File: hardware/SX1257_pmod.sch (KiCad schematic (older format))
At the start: 55 parts, among them J1 Conn_02x06_Odd_Even, J2 SMA_F_RX, J3 SMA_F_TX, U1 SX1257, U2 SC18IS602B, Y1 32/36MHz ?ppm

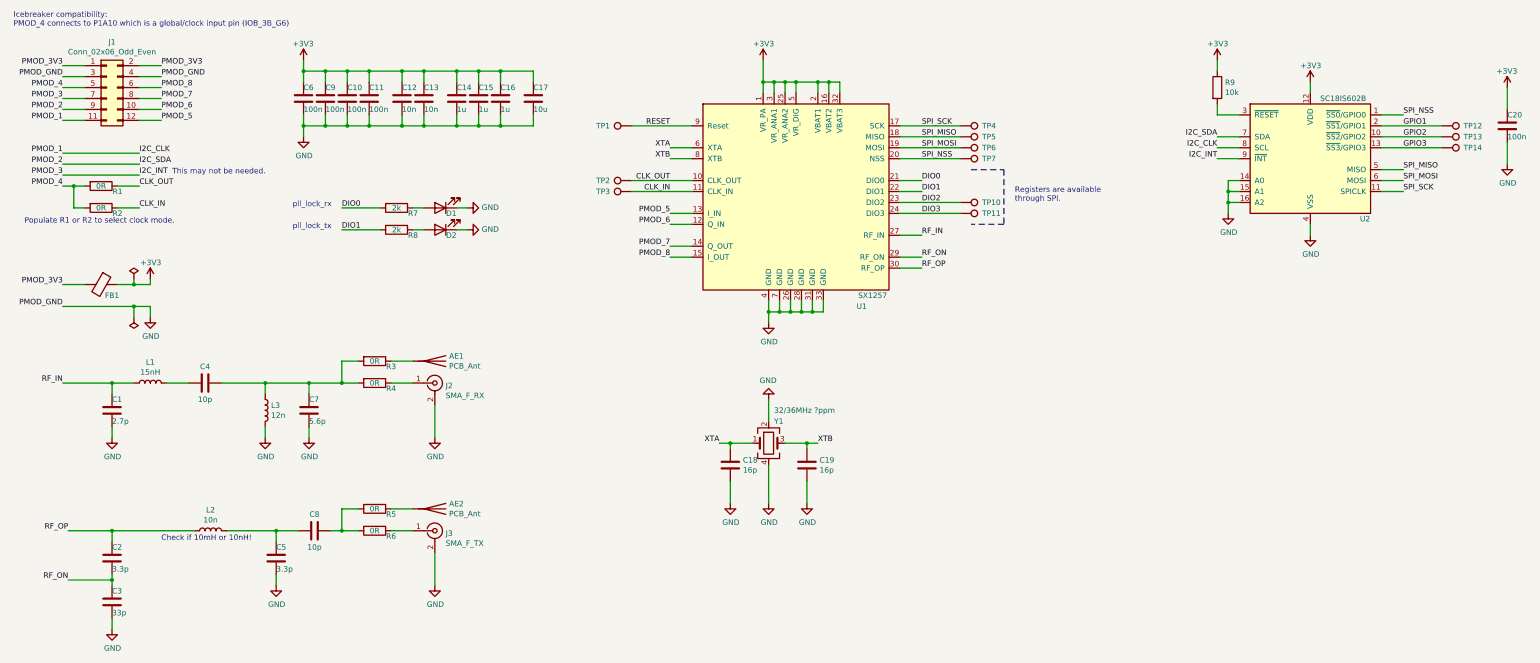
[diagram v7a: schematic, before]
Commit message: Some improvements and pcb work
- Connected gpio1 to SX_RESET
- Removed R0 for CLK select
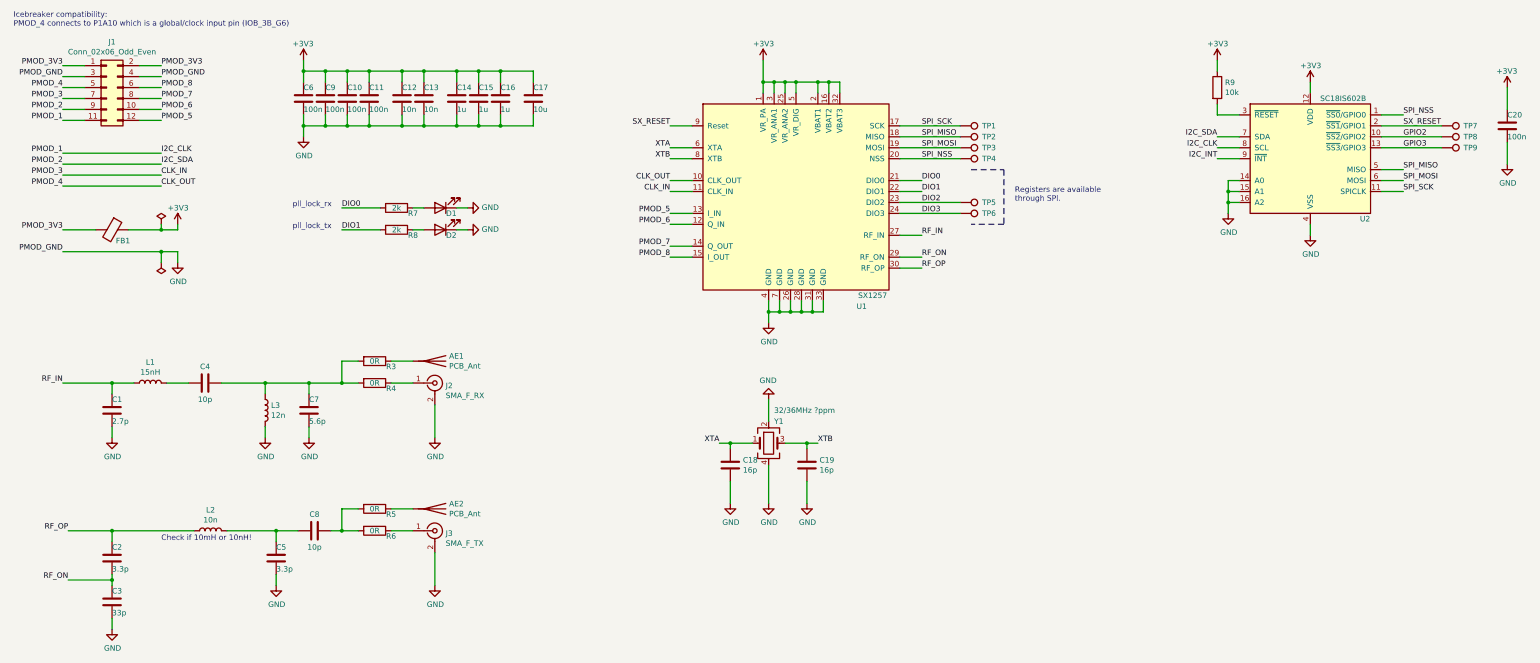
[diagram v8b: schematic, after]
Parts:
- removed R1, R2: 0R, Resistor_SMD:R_0603_1608Metric, symbol Device:R
- removed TP1, TP2, TP3: TestPoint, TestPoint:TestPoint_Pad_D1.0mm, symbol Connector:TestPoint
- renumbered TP4 to TP1, TP5 to TP2, TP6 to TP3, TP7 to TP4, TP10 to TP5, TP11 to TP6, TP12 to TP7, TP13 to TP8, TP14 to TP9
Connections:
- net PMOD_4 is gone; now on net CLK_OUT: J1.5 (Pin_5)
- net RESET is gone; now on net SX_RESET: U1.9 (Reset)
- net CLK_IN: now also J1.7 (Pin_7)
- net I2C_INT: no longer J1.7 (Pin_7)
- net GPIO1 renamed SX_RESET
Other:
- note removed: "Populate R1 or R2 to select clock mode."
- note removed: "This may not be needed."
- moved on the sheet: FB1
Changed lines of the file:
@@
 Text Label 1000 2150 2    50   ~ 0
 PMOD_4
-$Comp
-L Device:R R1
-U 1 1 5C2B7109
-P 1350 2150
-F 0 "R1" V 1400 2300 50  0000 C CNN
-F 1 "0R" V 1350 2150 50  0000 C CNN
-F 2 "Resistor_SMD:R_0603_1608Metric" V 1280 2150 50  0001 C CNN
-F 3 "~" H 1350 2150 50  0001 C CNN
-	1    1350 2150
-	0    1    1    0
-$EndComp
-Text Label 1700 2350 0    50   ~ 0
+Text Label 1900 2050 0    50   ~ 0
 CLK_IN
-Wire Wire Line
-	1000 2150 1100 2150
-Wire Wire Line
-	1500 2150 1700 2150
 Wire Wire Line
 	6750 1800 6550 1800
@@
 Wire Wire Line
 	1000 1050 1200 1050
-Text Label 1000 3050 2    50   ~ 0
+Text Label 1000 2550 2    50   ~ 0
 PMOD_3V3
 $Comp
 L Device:Ferrite_Bead FB1
 U 1 1 5C30A1D4
-P 1350 3050
-F 0 "FB1" V 1450 3150 50  0000 C CNN
-F 1 "Ferrite_Bead" V 1150 3000 50  0001 C CNN
-F 2 "Inductor_SMD:L_0603_1608Metric" V 1280 3050 50  0001 C CNN
-F 3 "~" H 1350 3050 50  0001 C CNN
-	1    1350 3050
-	0    1    1    0
-$EndComp
-Wire Wire Line
-	1000 3050 1200 3050
+P 1450 2550
+F 0 "FB1" V 1550 2650 50  0000 C CNN
+F 1 "Ferrite_Bead" V 1250 2500 50  0001 C CNN
+F 2 "Inductor_SMD:L_0603_1608Metric" V 1380 2550 50  0001 C CNN
+F 3 "~" H 1450 2550 50  0001 C CNN
+	1    1450 2550
+	0    1    1    0
+$EndComp
+Wire Wire Line
+	1000 2550 1300 2550
 $Comp
 L power:+3V3 #PWR03
 U 1 1 5C30B964
-P 1800 3000
-F 0 "#PWR03" H 1800 2850 50  0001 C CNN
-F 1 "+3V3" H 1700 3150 50  0000 L CNN
-F 2 "" H 1800 3000 50  0001 C CNN
-F 3 "" H 1800 3000 50  0001 C CNN
-	1    1800 3000
+P 2050 2500
+F 0 "#PWR03" H 2050 2350 50  0001 C CNN
+F 1 "+3V3" H 1950 2650 50  0000 L CNN
+F 2 "" H 2050 2500 50  0001 C CNN
+F 3 "" H 2050 2500 50  0001 C CNN
+	1    2050 2500
 	-1   0    0    -1
 $EndComp
@@
 L power:PWR_FLAG #FLG01
 U 1 1 5C3103FC
-P 1650 3000
-F 0 "#FLG01" H 1650 3075 50  0001 C CNN
-F 1 "PWR_FLAG" H 1650 3174 50  0001 C CNN
-F 2 "" H 1650 3000 50  0001 C CNN
-F 3 "~" H 1650 3000 50  0001 C CNN
-	1    1650 3000
-	1    0    0    -1
-$EndComp
-Wire Wire Line
-	1650 3000 1650 3050
-Connection ~ 1650 3050
-Wire Wire Line
-	1650 3050 1500 3050
-Wire Wire Line
-	1800 3050 1800 3000
-Wire Wire Line
-	1650 3050 1800 3050
+P 1900 2500
+F 0 "#FLG01" H 1900 2575 50  0001 C CNN
+F 1 "PWR_FLAG" H 1900 2674 50  0001 C CNN
+F 2 "" H 1900 2500 50  0001 C CNN
+F 3 "~" H 1900 2500 50  0001 C CNN
+	1    1900 2500
+	1    0    0    -1
+$EndComp
+Wire Wire Line
+	1900 2500 1900 2550
+Connection ~ 1900 2550
+Wire Wire Line
+	2050 2550 2050 2500
+Wire Wire Line
+	1900 2550 2050 2550
 Text Label 8850 2100 0    50   ~ 0
 DIO0
@@
 DIO3
 $Comp
-L Connector:TestPoint TP10
+L Connector:TestPoint TP5
 U 1 1 5C32BD15
 P 9200 2300
-F 0 "TP10" V 9200 2500 50  0000 L CNN
+F 0 "TP5" V 9200 2500 50  0000 L CNN
 F 1 "TestPoint" V 9200 2750 50  0001 L CNN
 F 2 "TestPoint:TestPoint_Pad_D1.0mm" H 9400 2300 50  0001 C CNN
@@
 $EndComp
 $Comp
-L Connector:TestPoint TP11
+L Connector:TestPoint TP6
 U 1 1 5C32DD47
 P 9200 2400
-F 0 "TP11" V 9200 2600 50  0000 L CNN
+F 0 "TP6" V 9200 2600 50  0000 L CNN
 F 1 "TestPoint" V 9200 2850 50  0001 L CNN
 F 2 "TestPoint:TestPoint_Pad_D1.0mm" H 9400 2400 50  0001 C CNN
@@
 L power:PWR_FLAG #FLG02
 U 1 1 5C3953E6
-P 1650 3350
-F 0 "#FLG02" H 1650 3425 50  0001 C CNN
-F 1 "PWR_FLAG" H 1650 3524 50  0001 C CNN
-F 2 "" H 1650 3350 50  0001 C CNN
-F 3 "~" H 1650 3350 50  0001 C CNN
-	1    1650 3350
+P 1900 2850
+F 0 "#FLG02" H 1900 2925 50  0001 C CNN
+F 1 "PWR_FLAG" H 1900 3024 50  0001 C CNN
+F 2 "" H 1900 2850 50  0001 C CNN
+F 3 "~" H 1900 2850 50  0001 C CNN
+	1    1900 2850
 	-1   0    0    1
 $EndComp
-$Comp
-L Connector:TestPoint TP1
-U 1 1 5C39E2AB
-P 6200 1600
-F 0 "TP1" V 6200 1800 50  0000 L CNN
-F 1 "TestPoint" V 6200 2050 50  0001 L CNN
-F 2 "TestPoint:TestPoint_Pad_D1.0mm" H 6400 1600 50  0001 C CNN
-F 3 "~" H 6400 1600 50  0001 C CNN
-	1    6200 1600
-	0    -1   -1   0
-$EndComp
-Text Label 6550 1600 2    50   ~ 0
-RESET
 Wire Wire Line
 	8650 2600 8850 2600
@@
 Wire Wire Line
 	1700 1150 1900 1150
-Text Label 1000 3250 2    50   ~ 0
+Text Label 1000 2750 2    50   ~ 0
 PMOD_GND
 $Comp
 L power:GND #PWR04
 U 1 1 5C3092FD
-P 1800 3350
-F 0 "#PWR04" H 1800 3100 50  0001 C CNN
-F 1 "GND" H 1805 3177 50  0000 C CNN
-F 2 "" H 1800 3350 50  0001 C CNN
-F 3 "" H 1800 3350 50  0001 C CNN
-	1    1800 3350
-	1    0    0    -1
-$EndComp
-Wire Wire Line
-	1000 3250 1650 3250
-Wire Wire Line
-	1800 3250 1800 3350
-Wire Wire Line
-	1650 3350 1650 3250
-Connection ~ 1650 3250
-Wire Wire Line
-	1650 3250 1800 3250
-Text Notes 650  2500 0    50   ~ 0
-Populate R1 or R2 to select clock mode.
-$Comp
-L Connector:TestPoint TP2
-U 1 1 5C3476A4
-P 6200 2100
-F 0 "TP2" V 6200 2300 50  0000 L CNN
-F 1 "TestPoint" V 6200 2550 50  0001 L CNN
-F 2 "TestPoint:TestPoint_Pad_D1.0mm" H 6400 2100 50  0001 C CNN
-F 3 "~" H 6400 2100 50  0001 C CNN
-	1    6200 2100
-	0    -1   -1   0
-$EndComp
-$Comp
-L Connector:TestPoint TP3
-U 1 1 5C34771A
-P 6200 2200
-F 0 "TP3" V 6200 2400 50  0000 L CNN
-F 1 "TestPoint" V 6200 2650 50  0001 L CNN
-F 2 "TestPoint:TestPoint_Pad_D1.0mm" H 6400 2200 50  0001 C CNN
-F 3 "~" H 6400 2200 50  0001 C CNN
-	1    6200 2200
-	0    -1   -1   0
-$EndComp
-Wire Wire Line
-	6200 1600 6750 1600
-Wire Wire Line
-	6200 2100 6750 2100
-Wire Wire Line
-	6200 2200 6750 2200
+P 2050 2850
+F 0 "#PWR04" H 2050 2600 50  0001 C CNN
+F 1 "GND" H 2055 2677 50  0000 C CNN
+F 2 "" H 2050 2850 50  0001 C CNN
+F 3 "" H 2050 2850 50  0001 C CNN
+	1    2050 2850
+	1    0    0    -1
+$EndComp
+Wire Wire Line
+	2050 2750 2050 2850
+Wire Wire Line
+	1900 2850 1900 2750
+Connection ~ 1900 2750
+Wire Wire Line
+	1900 2750 2050 2750
+Wire Wire Line
+	6550 1600 6750 1600
+Wire Wire Line
+	6550 2100 6750 2100
+Wire Wire Line
+	6550 2200 6750 2200
 Text Label 8850 1600 0    50   ~ 0
 SPI_SCK
 Text Label 13250 2200 0    50   ~ 0
 SPI_SCK
-$Comp
-L Device:R R2
-U 1 1 5C36ECA7
-P 1350 2350
-F 0 "R2" V 1400 2500 50  0000 C CNN
-F 1 "0R" V 1350 2350 50  0000 C CNN
-F 2 "Resistor_SMD:R_0603_1608Metric" V 1280 2350 50  0001 C CNN
-F 3 "~" H 1350 2350 50  0001 C CNN
-	1    1350 2350
-	0    1    1    0
-$EndComp
-Wire Wire Line
-	1700 2350 1500 2350
-Wire Wire Line
-	1200 2350 1100 2350
-Wire Wire Line
-	1100 2350 1100 2150
-Connection ~ 1100 2150
-Wire Wire Line
-	1100 2150 1200 2150
 Text Label 8850 1700 0    50   ~ 0
 SPI_MISO
@@
 Text Label 13250 1500 0    50   ~ 0
 SPI_NSS
-Wire Wire Line
-	1000 2050 1700 2050
-Wire Wire Line
-	1000 1950 1700 1950
-Wire Wire Line
-	1000 1850 1700 1850
-Text Label 1700 2150 0    50   ~ 0
+Text Label 1900 2150 0    50   ~ 0
 CLK_OUT
-Text Label 1700 1850 0    50   ~ 0
+Text Label 1900 1850 0    50   ~ 0
 I2C_CLK
-Text Label 1700 1950 0    50   ~ 0
+Text Label 1900 1950 0    50   ~ 0
 I2C_SDA
 $Comp
@@
 $EndComp
 $Comp
-L Connector:TestPoint TP4
+L Connector:TestPoint TP1
 U 1 1 5C309F67
 P 9200 1600
-F 0 "TP4" V 9200 1800 50  0000 L CNN
+F 0 "TP1" V 9200 1800 50  0000 L CNN
 F 1 "TestPoint" V 9200 2050 50  0001 L CNN
 F 2 "TestPoint:TestPoint_Pad_D1.0mm" H 9400 1600 50  0001 C CNN
@@
 	8650 1600 9200 1600
 $Comp
-L Connector:TestPoint TP5
+L Connector:TestPoint TP2
 U 1 1 5C3239F0
 P 9200 1700
-F 0 "TP5" V 9200 1900 50  0000 L CNN
+F 0 "TP2" V 9200 1900 50  0000 L CNN
 F 1 "TestPoint" V 9200 2150 50  0001 L CNN
 F 2 "TestPoint:TestPoint_Pad_D1.0mm" H 9400 1700 50  0001 C CNN
@@
 $EndComp
 $Comp
-L Connector:TestPoint TP6
+L Connector:TestPoint TP3
 U 1 1 5C323A5C
 P 9200 1800
-F 0 "TP6" V 9200 2000 50  0000 L CNN
+F 0 "TP3" V 9200 2000 50  0000 L CNN
 F 1 "TestPoint" V 9200 2250 50  0001 L CNN
 F 2 "TestPoint:TestPoint_Pad_D1.0mm" H 9400 1800 50  0001 C CNN
@@
 $EndComp
 $Comp
-L Connector:TestPoint TP7
+L Connector:TestPoint TP4
 U 1 1 5C323ACA
 P 9200 1900
-F 0 "TP7" V 9200 2100 50  0000 L CNN
+F 0 "TP4" V 9200 2100 50  0000 L CNN
 F 1 "TestPoint" V 9200 2350 50  0001 L CNN
 F 2 "TestPoint:TestPoint_Pad_D1.0mm" H 9400 1900 50  0001 C CNN
@@
 	13050 2200 13250 2200
 $Comp
-L Connector:TestPoint TP12
+L Connector:TestPoint TP7
 U 1 1 5C34614B
 P 13600 1600
-F 0 "TP12" V 13600 1800 50  0000 L CNN
+F 0 "TP7" V 13600 1800 50  0000 L CNN
 F 1 "TestPoint" V 13600 2050 50  0001 L CNN
 F 2 "TestPoint:TestPoint_Pad_D1.0mm" H 13800 1600 50  0001 C CNN
@@
 $EndComp
 $Comp
-L Connector:TestPoint TP13
+L Connector:TestPoint TP8
 U 1 1 5C346277
 P 13600 1700
-F 0 "TP13" V 13600 1900 50  0000 L CNN
+F 0 "TP8" V 13600 1900 50  0000 L CNN
 F 1 "TestPoint" V 13600 2150 50  0001 L CNN
 F 2 "TestPoint:TestPoint_Pad_D1.0mm" H 13800 1700 50  0001 C CNN
@@
 $EndComp
 $Comp
-L Connector:TestPoint TP14
+L Connector:TestPoint TP9
 U 1 1 5C3462EB
 P 13600 1800
-F 0 "TP14" V 13600 2000 50  0000 L CNN
+F 0 "TP9" V 13600 2000 50  0000 L CNN
 F 1 "TestPoint" V 13600 2250 50  0001 L CNN
 F 2 "TestPoint:TestPoint_Pad_D1.0mm" H 13800 1800 50  0001 C CNN
@@
 Text Label 11550 1900 2    50   ~ 0
 I2C_INT
-Text Label 1700 2050 0    50   ~ 0
-I2C_INT
-Text Notes 2000 2050 0    50   ~ 0
-This may not be needed.
 Text Notes 550  700  0    50   ~ 0
 Icebreaker compatibility:\nPMOD_4 connects to P1A10 which is a global/clock input pin (IOB_3B_G6)
@@
 Text Notes 3100 2550 0    50   ~ 0
 pll_lock_tx
-Text Label 13250 1600 0    50   ~ 0
-GPIO1
 Text Label 13250 1700 0    50   ~ 0
 GPIO2
@@
 	13050 1600 13600 1600
 Wire Wire Line
+	13050 1800 13600 1800
+Wire Wire Line
+	13050 1700 13600 1700
+Text Label 6550 1600 2    50   ~ 0
+SX_RESET
+Text Label 13250 1600 0    50   ~ 0
+SX_RESET
+Wire Wire Line
+	1000 1850 1900 1850
+Wire Wire Line
+	1000 1950 1900 1950
+Wire Wire Line
+	1000 2050 1900 2050
+Wire Wire Line
+	1000 2150 1900 2150
+Wire Wire Line
+	1600 2550 1900 2550
+Wire Wire Line
+	1000 2750 1900 2750
+Wire Wire Line
 	13050 1500 13250 1500
-Wire Wire Line
-	13050 1800 13600 1800
-Wire Wire Line
-	13050 1700 13600 1700
 $EndSCHEMATC
